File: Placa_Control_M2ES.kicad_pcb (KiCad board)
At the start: 2 copper layers, 204 x 108 mm, 291 parts, among them J1 Screw_Terminal_01x06, J10 Screw_Terminal_01x06, J11 Screw_Terminal_01x02, J13 Screw_Terminal_01x04, J2 Screw_Terminal_01x06, J3 Screw_Terminal_01x06, J4 Screw_Terminal_01x06, J5 Screw_Terminal_01x06, J6 Screw_Terminal_01x06, J7 ARJM11C7-009-AB-EW2, J8 Screw_Terminal_01x06, J9 Screw_Terminal_01x06, K1 HF46F-G, K10 HF46F-G, K11 HF46F-G, K12 HF46F-G, K2 HF46F-G, K3 HF46F-G, K4 HF46F-G, K5 HF46F-G, K6 HF46F-G, K7 HF46F-G, K8 HF46F-G, K9 HF46F-G, U1 ULN2003, U10 L78M08CDT-TR, U11 LD29150, U12 LAN8742A, U13 USBLC6-4SC6, U14 TLV9101, U15 TLV9101, U16 TLV9101, U17 TLV9101, U18 TLV9101, U19 TLV9101, U2 ULN2003, U20 TLV9101, U21 TLV9101, U22 REF3030, U24 STM32F407VGTx, U3 REF35102QDBVR, U4 ADS1256, U5 ADS1256, U6 TLV9101, U7 OKI-78SR-12_1.0-W36-C, U8 uA7810, U9 LD29150, Y1 8.0Mhz, Y2 8.0Mhz, Y3 25Mhz, Y4 8Mhz

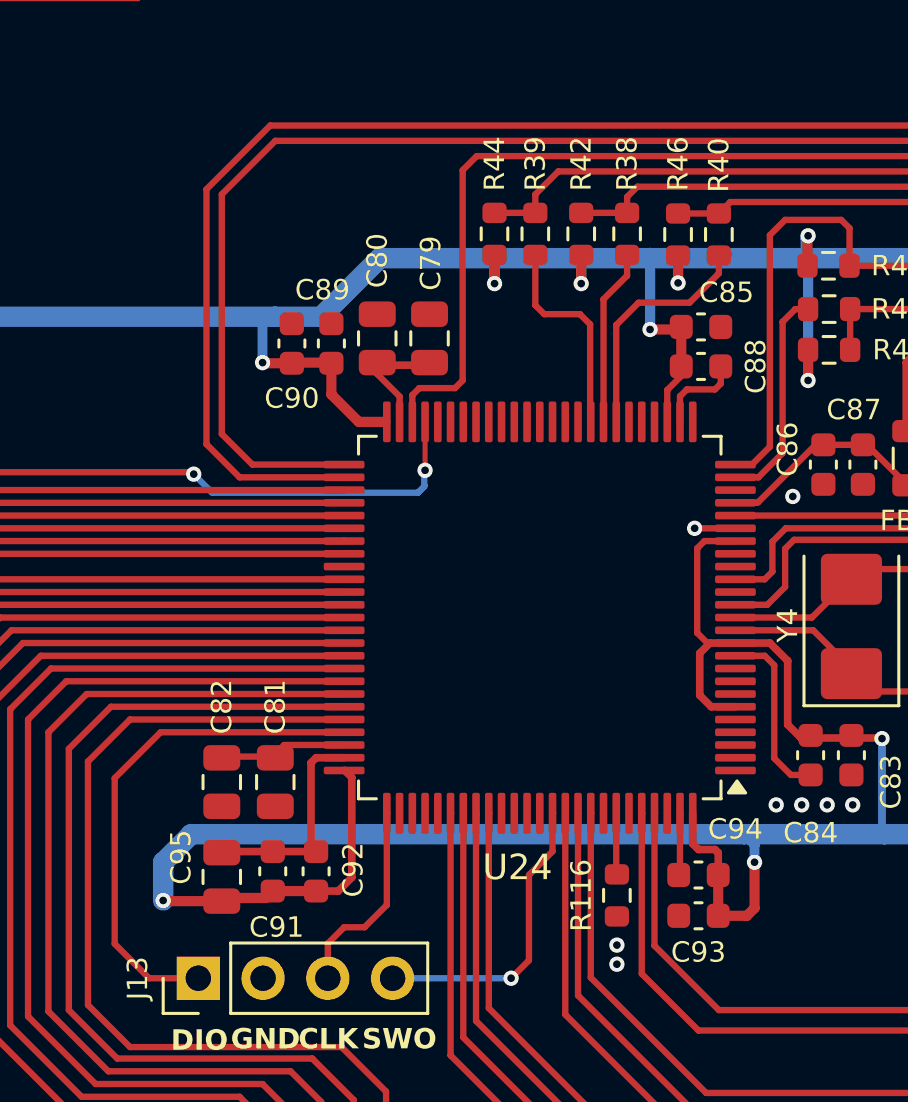
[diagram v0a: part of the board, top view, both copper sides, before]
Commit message: Se corrige el nombre para la ref de 2.5V para los canales análogos, Se corrigen quita un capacitor en cada pin VCAP, Se actualiza PCB
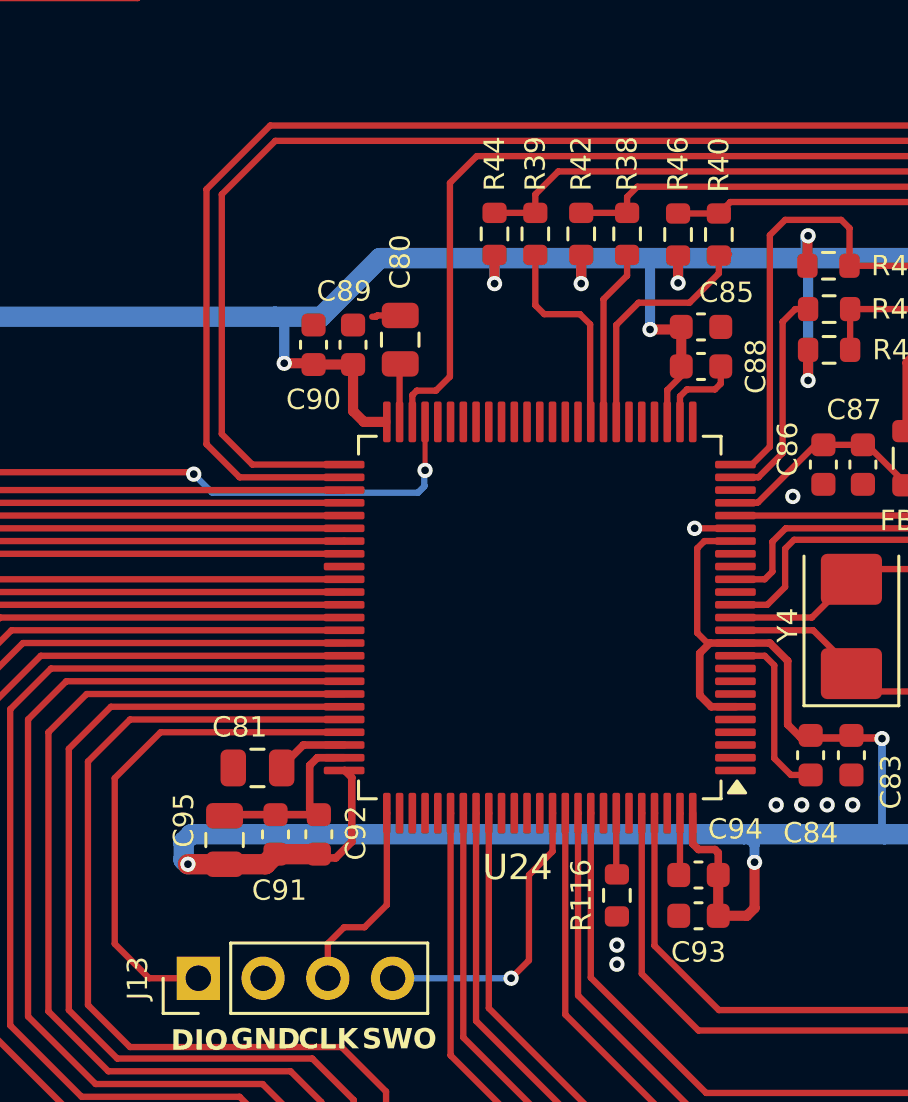
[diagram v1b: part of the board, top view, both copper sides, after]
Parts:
- removed C79, C82: 2u2F/50V, Capacitor_SMD:C_0805_2012Metric
- U3: value REF35102QDBVR -> REF35250QDBVR
- moved C92 1.45 mm to (182.1, 85.5)
- moved C91 1.45 mm to (180.4, 85.5)
- moved C95 1.45 mm to (178.4, 85.7)
- moved C80 0.90 mm to (185.3, 66.1)
- moved C81 0.89 mm to (179.7, 82.9), turned to 180 degrees
- moved C89 0.85 mm to (183.4, 66.3)
- moved C90 0.85 mm to (181.9, 66.3)
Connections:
- net Net-(U22-OUT) renamed /MCU/3V
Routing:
- net /3V3: track 554.1 -> 549.4 mm
- net Net-(U24-VCAP_1): track 4.88 -> 2.29 mm
- net Net-(U24-VCAP_2): track 5.42 -> 2.85 mm

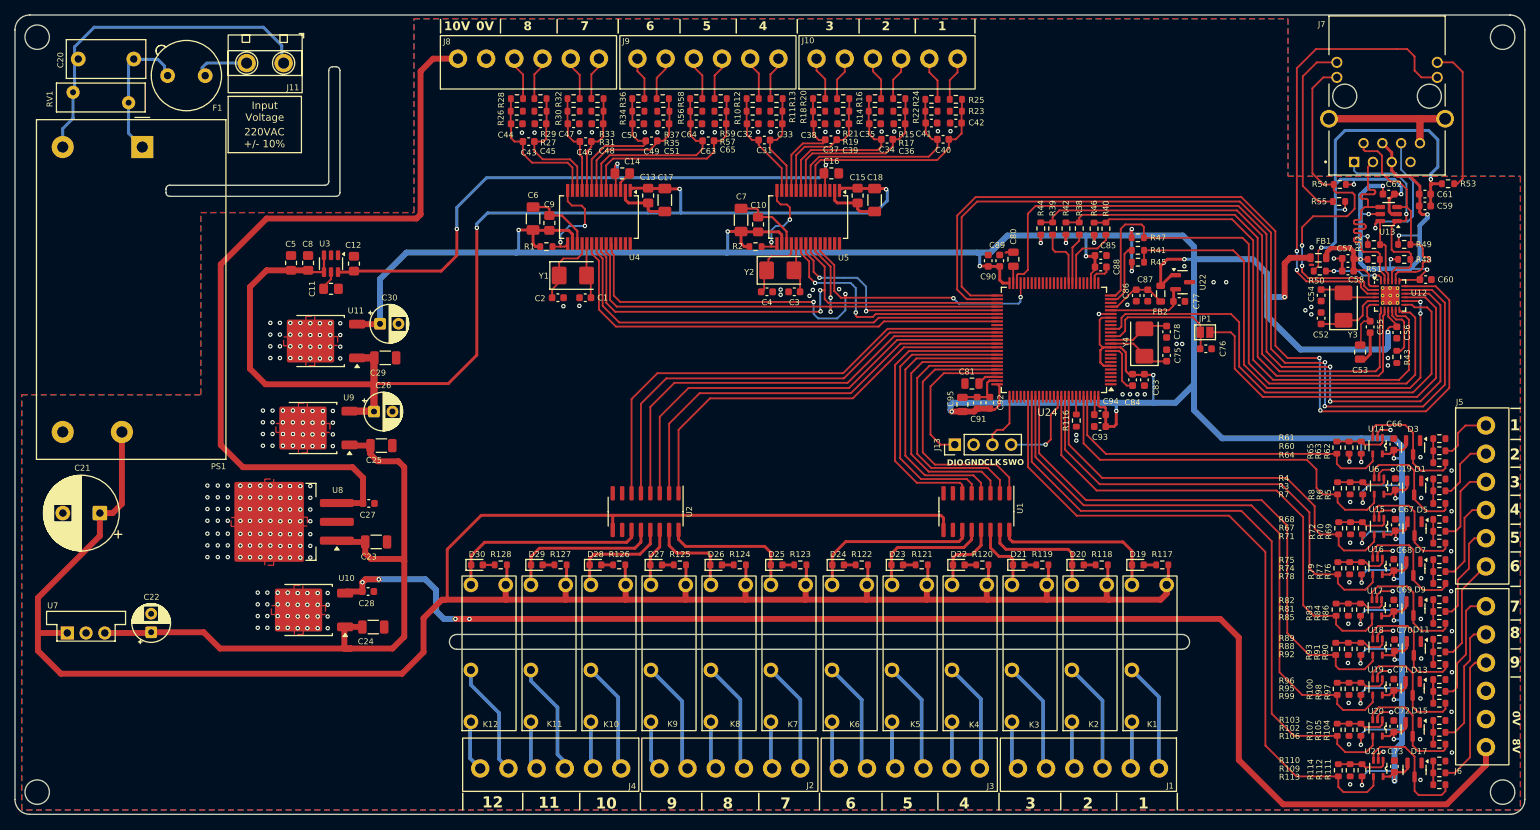
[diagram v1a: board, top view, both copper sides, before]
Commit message: Se añaden leds a la entrada de los Namur. Se estandariza y revisan varios footprints de los capacitores. El cambio no fue demasiado, se corrigio en placa. Se hacen algunos cambios adicionales a los valores. Se realiza un avance para jlcpcb
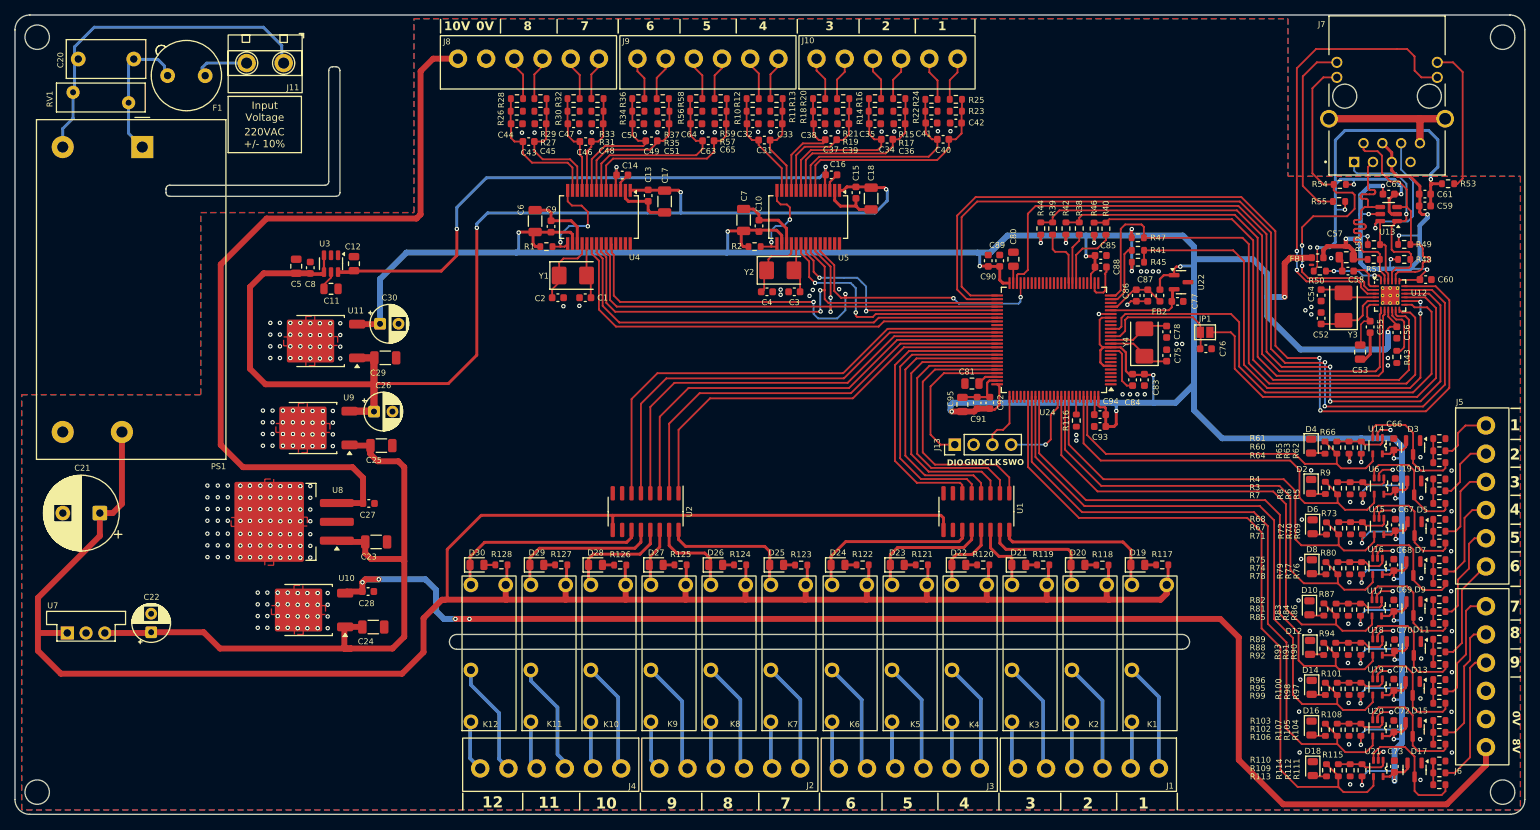
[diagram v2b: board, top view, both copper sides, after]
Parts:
- added D10: LED, LED_SMD:LED_0805_2012Metric, F.Cu at (225.3, 113.2)
- added D12: LED, LED_SMD:LED_0805_2012Metric, F.Cu at (225.3, 118.5)
- added D14: LED, LED_SMD:LED_0805_2012Metric, F.Cu at (225.6, 123.9)
- added D16: LED, LED_SMD:LED_0805_2012Metric, F.Cu at (225.5, 129.4)
- added D18: LED, LED_SMD:LED_0805_2012Metric, F.Cu at (225.7, 134.9)
- added D2: LED, LED_SMD:LED_0805_2012Metric, F.Cu at (225.5, 96.8)
- added D4: LED, LED_SMD:LED_0805_2012Metric, F.Cu at (225.5, 91.3)
- added D6: LED, LED_SMD:LED_0805_2012Metric, F.Cu at (225.7, 102.2)
- added D8: LED, LED_SMD:LED_0805_2012Metric, F.Cu at (225.6, 107.6)
- added R101: 10k, Resistor_SMD:R_0603_1608Metric, F.Cu at (227.4, 124.1)
- added R108: 10k, Resistor_SMD:R_0603_1608Metric, F.Cu at (227.4, 129.6)
- added R115: 10k, Resistor_SMD:R_0603_1608Metric, F.Cu at (227.6, 135.1)
- added R66: 10k, Resistor_SMD:R_0603_1608Metric, F.Cu at (227.4, 91.5)
- added R73: 10k, Resistor_SMD:R_0603_1608Metric, F.Cu at (227.6, 102.4)
- added R80: 10k, Resistor_SMD:R_0603_1608Metric, F.Cu at (227.5, 107.8)
- added R87: 10k, Resistor_SMD:R_0603_1608Metric, F.Cu at (227.2, 113.4)
- added R9: 10k, Resistor_SMD:R_0603_1608Metric, F.Cu at (227.4, 97.0)
- added R94: 10k, Resistor_SMD:R_0603_1608Metric, F.Cu at (227.2, 118.7)
- C10, C13, C14, C15, C16, C8, C9: footprint Resistor_SMD:R_0805_2012Metric_Pad1.20x1.40mm_HandSolder -> Capacitor_SMD:C_0603_1608Metric
- C11, C12, C5: footprint Resistor_SMD:R_0805_2012Metric_Pad1.20x1.40mm_HandSolder -> Capacitor_SMD:C_0805_2012Metric
- C17, C18, C6, C7: footprint Resistor_SMD:R_1206_3216Metric_Pad1.30x1.75mm_HandSolder -> Capacitor_SMD:C_1206_3216Metric
- C29: value 1uF 50V -> 1uF/50V
- C57: footprint Capacitor_SMD:C_0603_1608Metric -> Capacitor_SMD:C_0805_2012Metric
- D19, D20, D21, D22, D23, D24, D25, D26, D27, D28, D29, D30: footprint LED_SMD:LED_0603_1608Metric -> LED_SMD:LED_0805_2012Metric
- FB1, FB2: value 600R -> 450mR/200mA; footprint Inductor_SMD:L_0805_2012Metric -> Inductor_SMD:L_0603_1608Metric
- R1, R2: value 100 -> 1k
- R47: value 1k5 -> 1k
- R53, R55: value 510R -> 10k
- moved C5 0.83 mm to (88.4, 67.0)
- moved C8 0.72 mm to (90.3, 67.2)
- moved C9 0.53 mm to (122.8, 61.6)
- moved C18 0.52 mm to (166.0, 57.9)
- moved C15 0.46 mm to (164.0, 57.1)
- moved C6 0.45 mm to (120.6, 60.9)
- moved C7 0.35 mm to (148.8, 60.8)
- moved C57 0.29 mm to (230.2, 65.8)
- moved FB2 0.27 mm to (205.1, 71.0)
- moved C10 0.24 mm to (150.9, 61.6)
- moved C14 0.23 mm to (132.4, 54.7)
- moved C77 0.22 mm to (207.4, 71.8)
- moved C17 0.20 mm to (138.1, 58.3)
- moved U22 0.20 mm to (207.9, 69.2)
- moved C16 0.20 mm to (160.7, 54.7)
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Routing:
- net GND: track 158.3 -> 173.5 mm, vias 256 -> 265
- net /Digital Inputs/DIG_3: track 57.8 -> 62.8 mm
- net /Digital Inputs/DIG_9: track 92.1 -> 97.0 mm
- net /Digital Inputs/DIG_6: track 75.4 -> 79.9 mm
- net /Digital Inputs/DIG_4: track 63.2 -> 67.4 mm
- net /Digital Inputs/DIG_7: track 81.0 -> 85.1 mm
- net /Digital Inputs/DIG_5: track 68.9 -> 73.0 mm
- net /Digital Inputs/DIG_2: track 52.9 -> 56.7 mm
- net /Digital Inputs/DIG_8: track 87.1 -> 90.8 mm
- net /Digital Inputs/DIG_1: track 47.9 -> 50.8 mm
- net /Ethernet/VDD_LAN_F_3V3: track 75.8 -> 78.1 mm
- net Net-(D2-A): track 0.00 -> 2.03 mm
- net Net-(D10-A): track 0.00 -> 2.00 mm
- net /3V3: track 549.4 -> 547.4 mm
- net Net-(D8-A): track 0.00 -> 1.94 mm
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
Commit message: Se añade led de status y eeprom externa. Se actualiza pcb y se añade serigrafía adicional. Se actualiza los componentes jlcpcb, se utiliza un micro con con 512kbytes de flash a recomendacion de jefry debido a la escasez de los de 1024 kbytes. Se revisa y se espera mandar a china
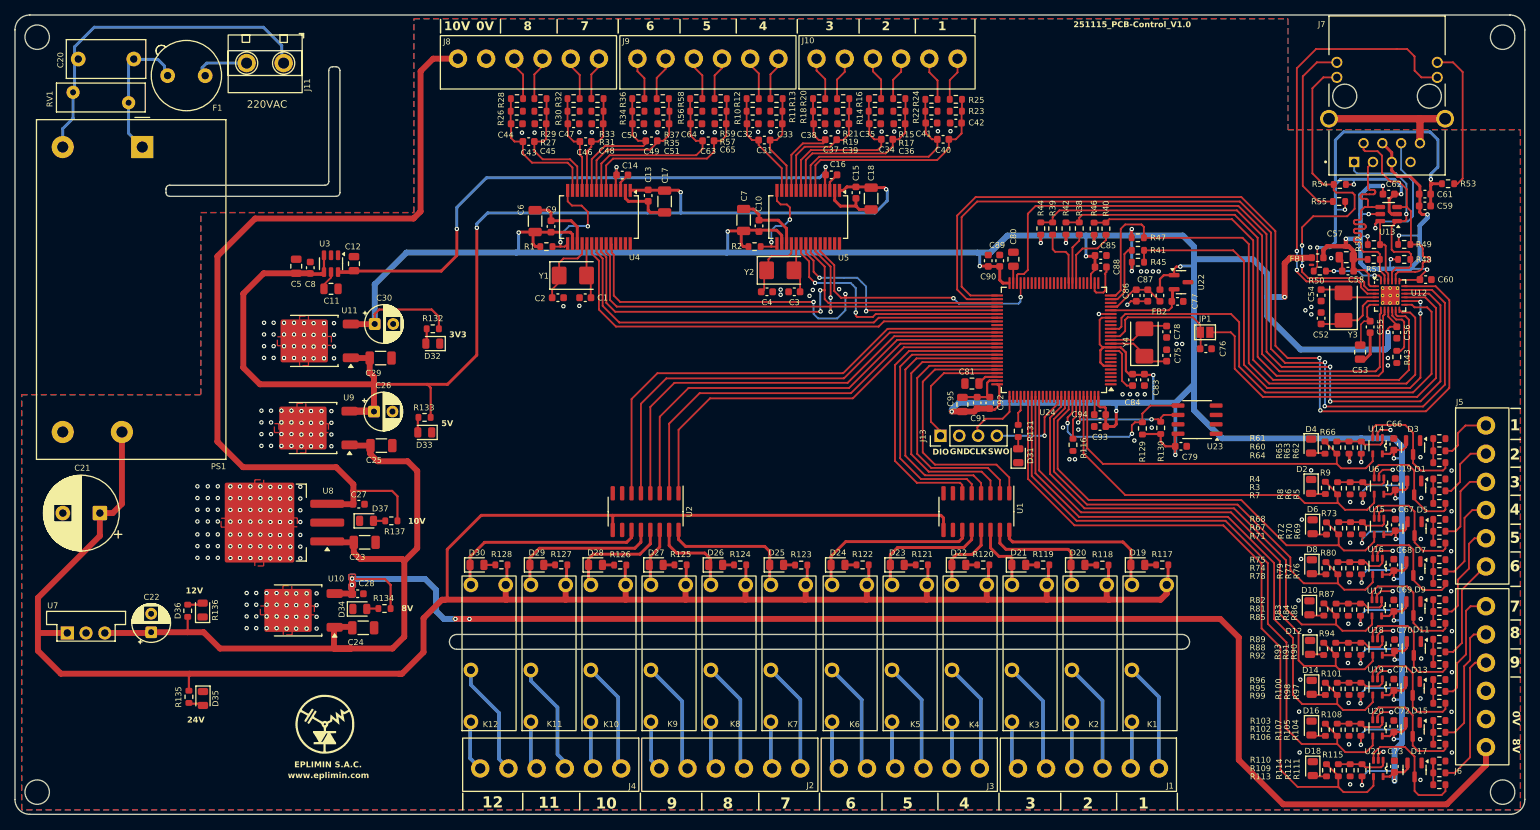
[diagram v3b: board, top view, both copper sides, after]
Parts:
- added C79: 100nF/50V, 1-Capacitor:C_0603_1608Metric, F.Cu at (207.9, 91.3)
- added D31: LED, LED_SMD:LED_0805_2012Metric, F.Cu at (185.9, 92.6)
- added D32: LED, LED_SMD:LED_0805_2012Metric, F.Cu at (106.8, 77.5)
- added D33: LED, LED_SMD:LED_0805_2012Metric, F.Cu at (105.7, 89.5)
- added D34: LED, LED_SMD:LED_0805_2012Metric, F.Cu at (97.0, 113.3)
- added D35: LED, LED_SMD:LED_0805_2012Metric, F.Cu at (75.8, 125.4)
- added D36: LED, LED_SMD:LED_0805_2012Metric, F.Cu at (75.7, 113.5)
- added D37: LED, LED_SMD:LED_0805_2012Metric, F.Cu at (97.9, 101.4)
- added G1: LOGO, LOGO, F.Cu at (92.2, 128.9)
- added R129: 2k2, Resistor_SMD:R_0603_1608Metric, F.Cu at (202.7, 88.9)
- added R130: 2k2, Resistor_SMD:R_0603_1608Metric, F.Cu at (205.2, 88.8)
- added R131: 5k1, Resistor_SMD:R_0603_1608Metric, F.Cu at (185.9, 89.3)
- added R132: 5k1, Resistor_SMD:R_0603_1608Metric, F.Cu at (106.8, 75.5)
- added R133: 5k1, Resistor_SMD:R_0603_1608Metric, F.Cu at (105.7, 87.4)
- added R134: 5k1, Resistor_SMD:R_0603_1608Metric, F.Cu at (100.3, 113.3)
- added R135: 10k, Resistor_SMD:R_0603_1608Metric, F.Cu at (73.9, 125.2)
- added R136: 10k, Resistor_SMD:R_0603_1608Metric, F.Cu at (73.7, 113.6)
- added R137: 10k, Resistor_SMD:R_0603_1608Metric, F.Cu at (101.2, 101.4)
- added U23: 24xx256, Package_SO:SO-8_3.9x4.9mm_P1.27mm, F.Cu at (210.1, 87.7)
- U11: value LD29150 -> LD29150DT33R
- U9: value LD29150 -> LD29150DT50R
- moved R116 3.31 mm to (193.3, 91.1)
- moved J13 2.27 mm to (175.4, 89.9)
- moved C23 1.55 mm to (97.6, 104.3)
- moved C28 1.44 mm to (96.7, 111.3)
- moved U10 1.42 mm to (88.5, 113.5)
- moved C24 1.37 mm to (97.4, 115.9)
- moved C27 1.35 mm to (96.8, 99.2)
- moved U8 1.30 mm to (84.9, 101.6)
- moved U11 0.85 mm to (90.7, 77.1)
- moved C30 0.73 mm to (99.0, 74.8)
- moved C29 0.63 mm to (99.8, 79.4)
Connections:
- U24 pad 79: unconnected-(U24-PC11-Pad79) -> /MCU/LED_STATUS
- U24 pad 93: unconnected-(U24-PB7-Pad93) -> /MCU/MCU_I2C1_SDA
- U24 pad 95: unconnected-(U24-PB8-Pad95) -> /MCU/MCU_I2C1_SCL
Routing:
- net /3V3: track 547.4 -> 574.5 mm, vias 33 -> 34
- net /MCU/MCU_I2C1_SDA: track 0.00 -> 23.3 mm, vias 0 -> 2
- net /MCU/MCU_I2C1_SCL: track 0.00 -> 18.2 mm, vias 0 -> 2
- net /10V: track 107.4 -> 116.3 mm
- net /8V: track 188.5 -> 196.9 mm
- net /Fuente/12V: track 91.7 -> 98.6 mm
- net /5V: track 162.8 -> 169.1 mm
- net /MCU/LED_STATUS: track 0.00 -> 3.93 mm
- net Net-(U24-BOOT0): track 2.42 -> 5.87 mm
- net /MCU/SWDIO: track 20.1 -> 16.9 mm
- net /24V: track 334.8 -> 337.1 mm
- net /Digital Inputs/DIG_6: track 79.9 -> 77.6 mm
- net Net-(D36-A): track 0.00 -> 2.10 mm
- net /Digital Inputs/DIG_7: track 85.1 -> 83.0 mm
- net Net-(D33-A): track 0.00 -> 2.07 mm
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- added copper zone on B.Cu, net /8V
- added copper zone on F.Cu, net /8V
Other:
- board text added: "12V"
- board text added: "220VAC"
- board text added: "24V"
- board text added: "251115_PCB-Control_V1.0"
- board text added: "3V3"
- board text added: "5V"
- board text added: "EPLIMIN S.A.C."
- board text added: "www.eplimin.com"
- board text removed: "220VAC +/- 10%"
- board text removed: "Input Voltage"
